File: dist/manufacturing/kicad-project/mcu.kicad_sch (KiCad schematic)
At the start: 22 parts, among them SW1 SW1, U16 STM32G0B1CBT6, U17 W25Q32JVSSIQ, Y1 Y1

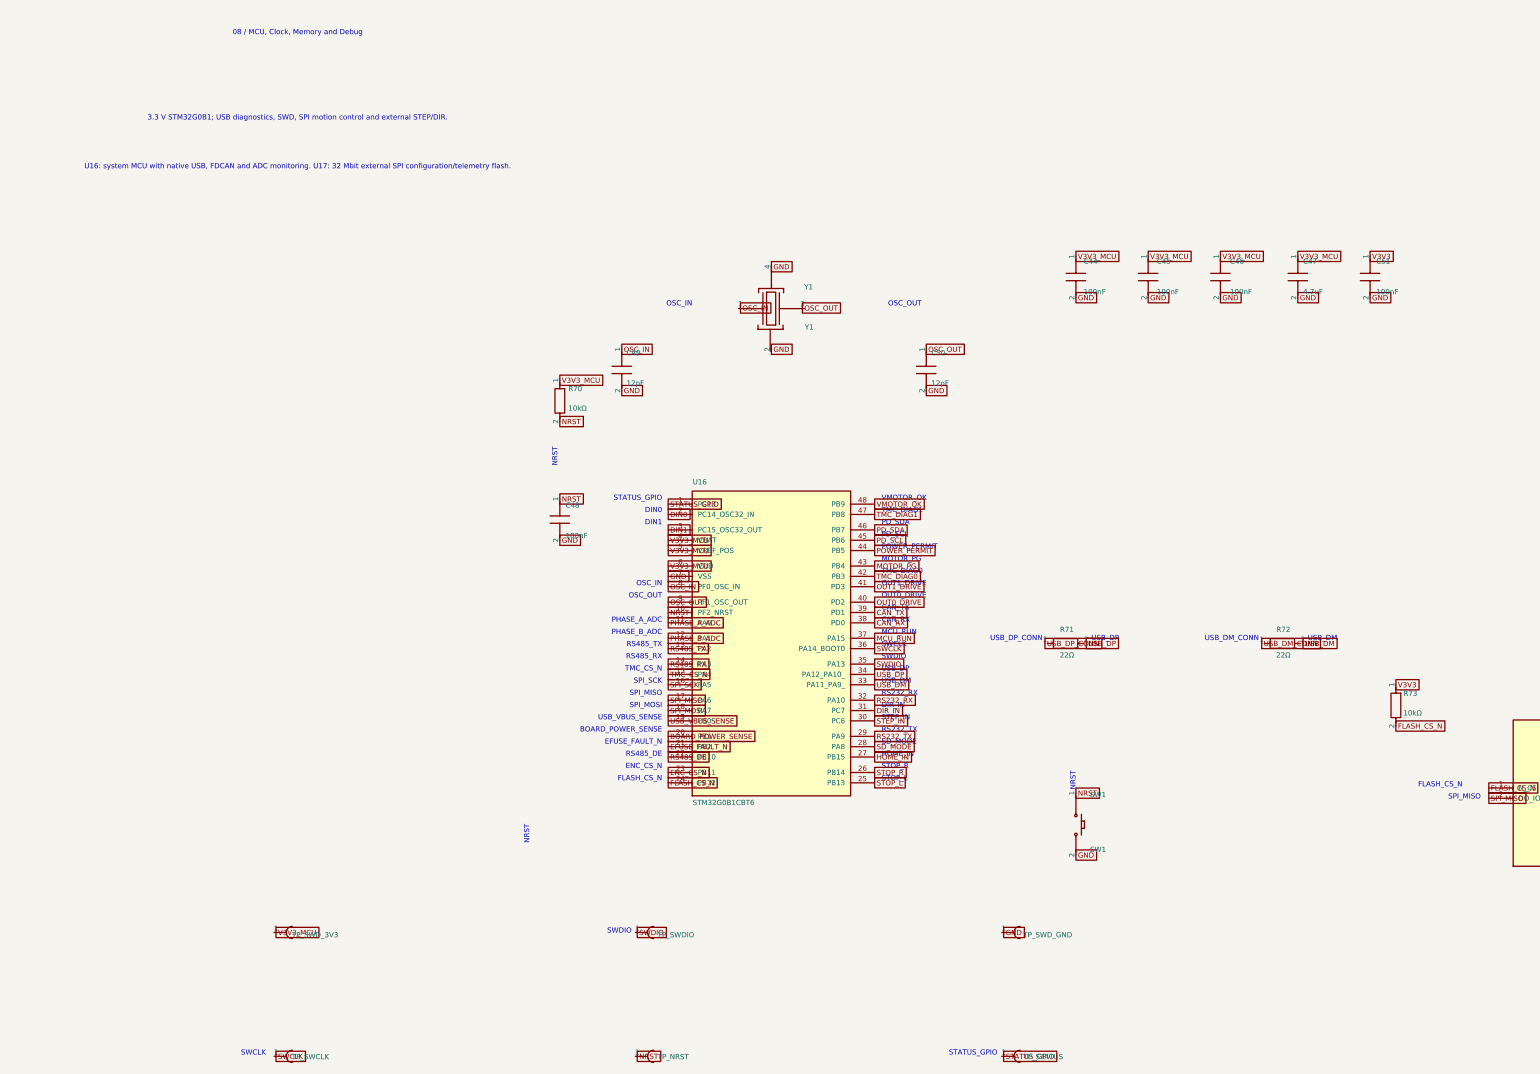
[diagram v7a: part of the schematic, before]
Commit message: Fix source warnings and organize schematic on A4 sheets
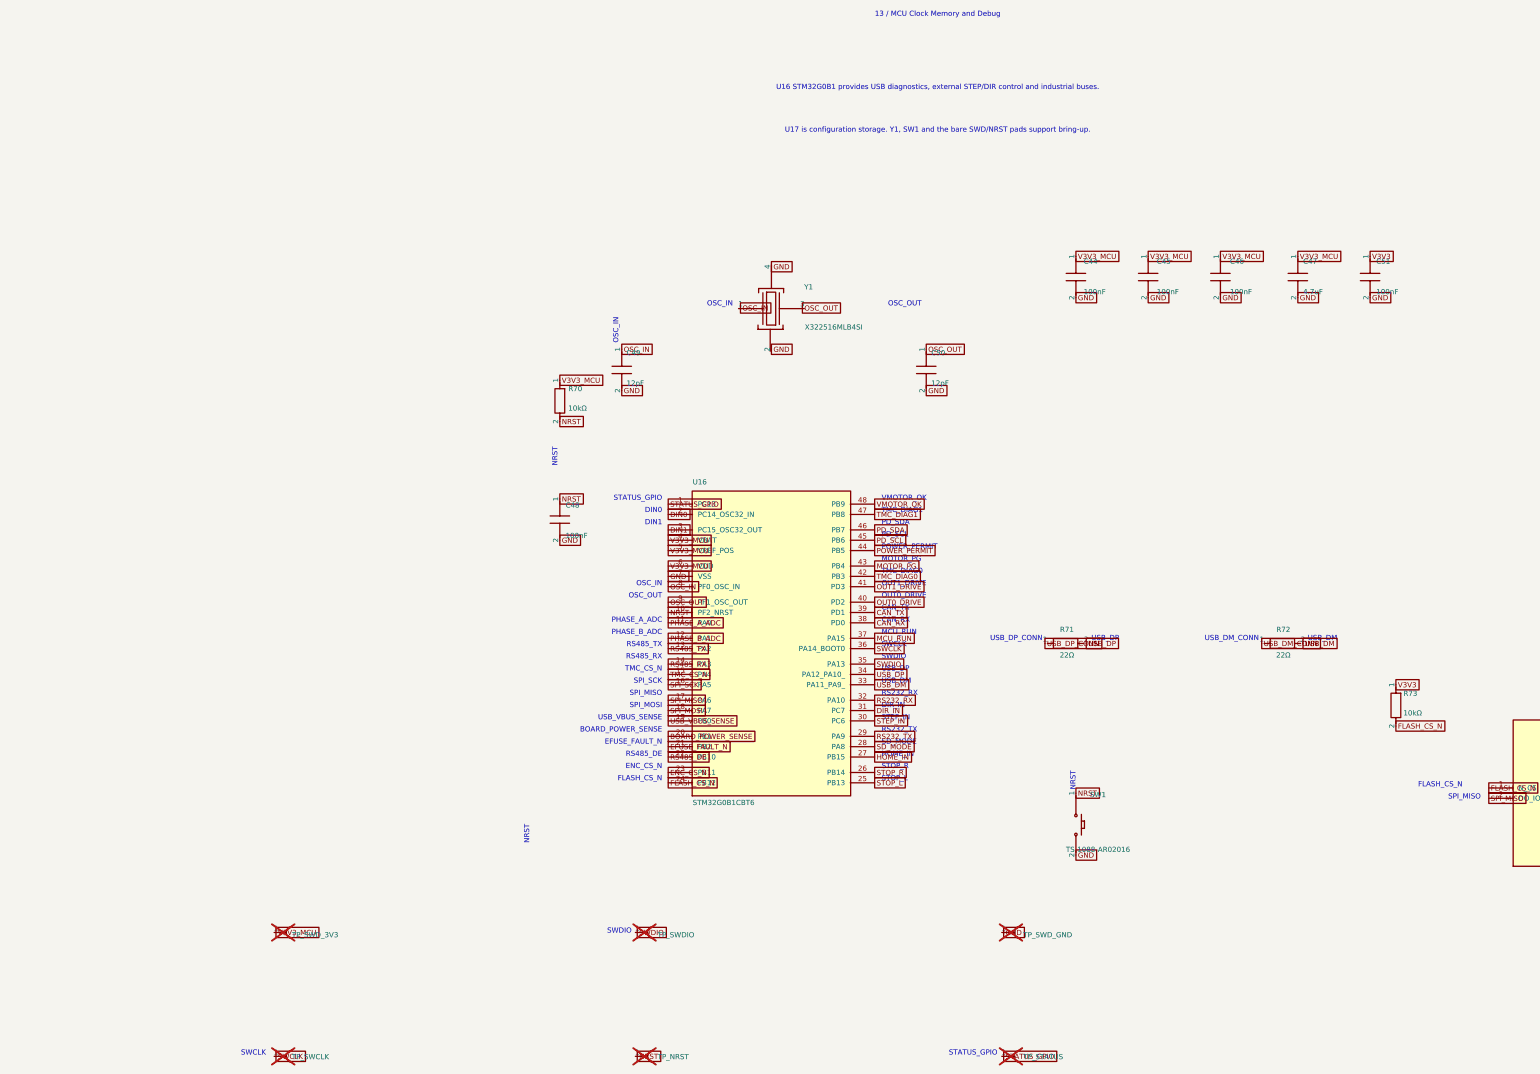
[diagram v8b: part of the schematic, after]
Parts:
- SW1: value SW1 -> TS-1088-AR02016
- TP_NRST, TP_STATUS, TP_SWCLK, TP_SWDIO, TP_SWD_3V3, TP_SWD_GND: now not fitted; now left out of the parts list
- Y1: value Y1 -> X322516MLB4SI
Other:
- note added: "13 / MCU Clock Memory and Debug"
- note added: "U16 STM32G0B1 provides USB diagnostics, external STEP/DIR control and industrial buses."
- note added: "U17 is configuration storage. Y1, SW1 and the bare SWD/NRST pads support bring-up."
- note removed: "08 / MCU, Clock, Memory and Debug"
- note removed: "3.3 V STM32G0B1; USB diagnostics, SWD, SPI motion control and external STEP/DIR."
- note removed: "U16: system MCU with native USB, FDCAN and ADC monitoring. U17: 32 Mbit external SPI configuration/telemetry flash."
